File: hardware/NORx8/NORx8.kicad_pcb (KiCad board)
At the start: 2 copper layers, 53.3 x 86.4 mm, 8 parts, among them J1 Left, J2 Right, J3 DBG, J4 Left, J5 Right

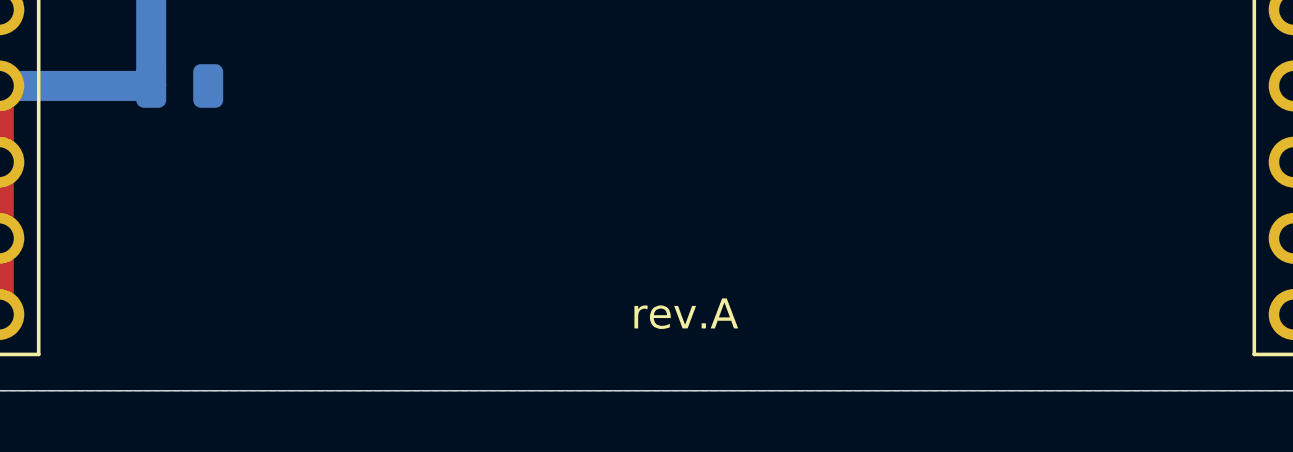
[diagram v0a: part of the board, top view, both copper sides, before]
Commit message: hardware: update top board labels
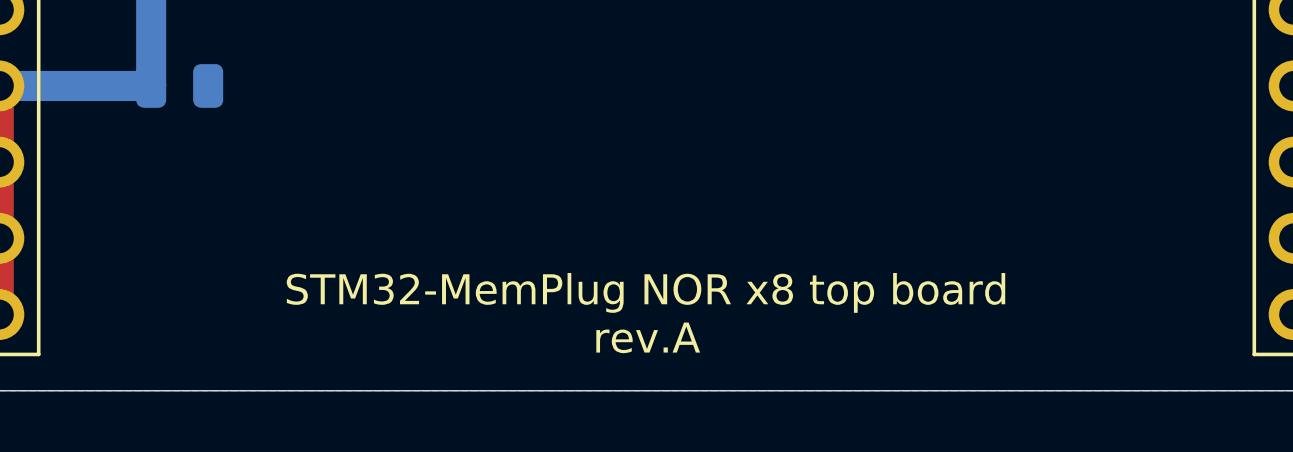
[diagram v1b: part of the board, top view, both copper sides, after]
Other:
- board text added: "STM32-MemPlug NOR x8 top board rev.A"
- board text removed: "rev.A"

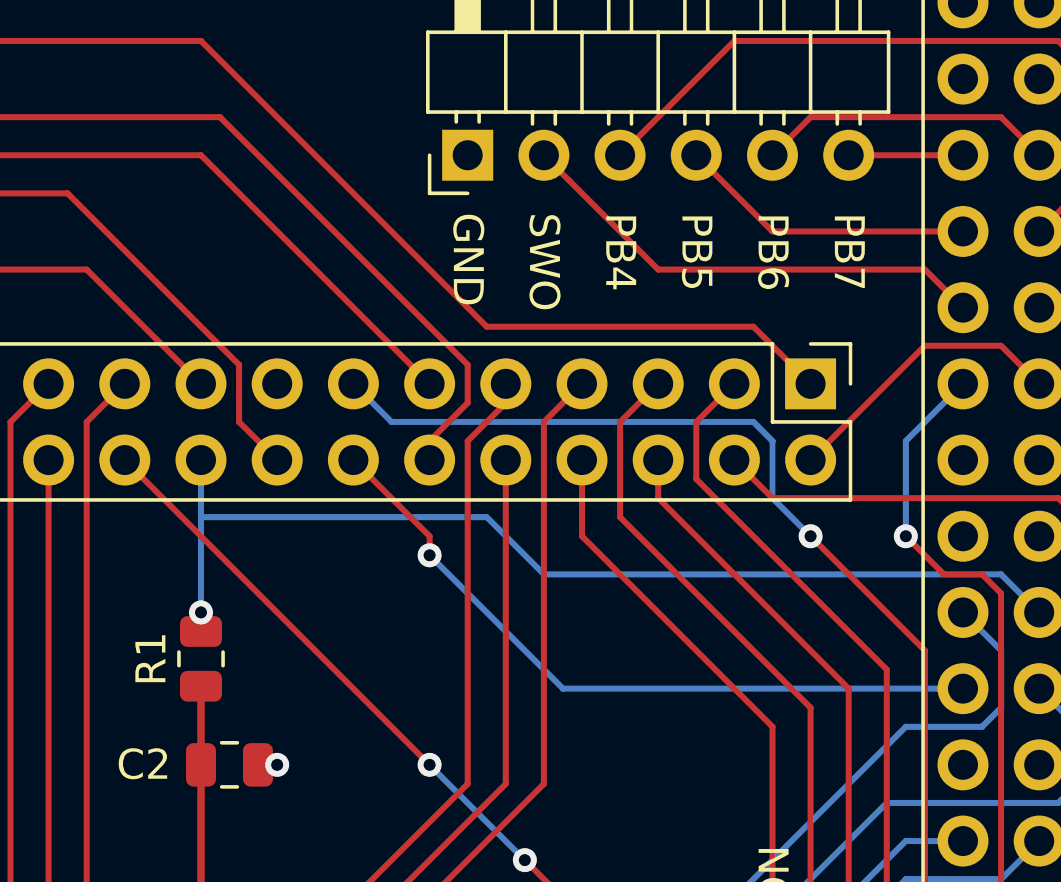
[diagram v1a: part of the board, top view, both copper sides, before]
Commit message: refreshed carrier boards and added missing symbol libs
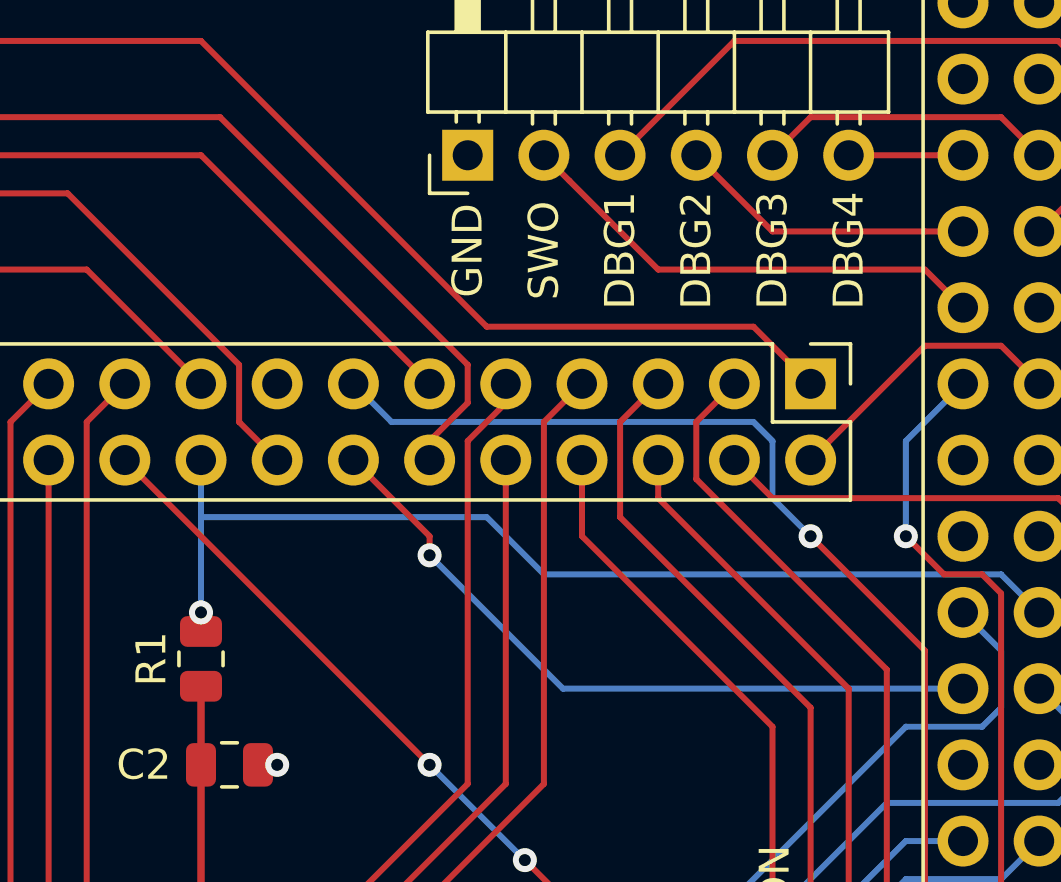
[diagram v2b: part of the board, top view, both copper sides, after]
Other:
- board text added: "DBG1"
- board text added: "DBG2"
- board text added: "DBG3"
- board text added: "DBG4"
- board text removed: "PB4"
- board text removed: "PB5"
- board text removed: "PB6"
- board text removed: "PB7"
